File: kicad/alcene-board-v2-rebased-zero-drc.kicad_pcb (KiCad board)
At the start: 2 copper layers, 109.3 x 87.1 mm, 16 parts, among them J1 ESP32-S3-DevKitC-1_J1, J2 USB-C Input, J3 ESP32-S3-DevKitC-1_J3, J4 ILI9341_TFT_14pin, J5 Male Pin Header 1x18 - J1 Sig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, J6 Male Pin Header 1x18 - J3 Sig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, J7 Male Pin Header 2x4 - GND, J8 Male Pin Header 2x4 - 3V3, J9 Male Pin Header 2x4 - VIN 5V, SW1 ESP32-S3 Reset (NO momentary)

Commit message: feat: moving R and C positions
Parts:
- moved C1 25.5 mm to (123.0, 114.5), turned to -90 degrees
- moved C2 24.6 mm to (128.0, 114.5), turned to -90 degrees
- moved R2 23.8 mm to (126.2, 110.2)
- moved R1 23.4 mm to (121.7, 110.2)
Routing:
- net GND: track 240.2 -> 272.8 mm
- net Net-(J2-PadA5): track 2.33 -> 27.3 mm, vias 0 -> 2
- net VIN: track 167.5 -> 183.0 mm, vias 1 -> 3
- net Net-(J2-PadB5): track 10.2 -> 25.1 mm, vias 0 -> 1
- net GPIO19: track 51.3 -> 50.8 mm

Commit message: feat: update layouting
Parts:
- moved J7 1.27 mm to (129.7, 38.8)
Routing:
- net GND: track 272.8 -> 274.0 mm
- net GPIO14: track 75.4 -> 74.8 mm
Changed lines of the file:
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@@
 		(tags "USB Type-C Receptacle Through-hole Right angle")
 		(property "Reference" "J2"
-			(at 10.605 -4.49 0)
+			(at 3.355 -1.94 0)
 			(layer "F.SilkS")
 			(effects
@@
 	(footprint "Connector_PinHeader_2.54mm:PinHeader_2x04_P2.54mm_Vertical"
 		(layer "F.Cu")
-		(at 130.93 38.75 -90)
+		(at 129.66 38.75 -90)
 		(descr "Through hole straight pin header, 2x04, 2.54mm pitch, double rows")
 		(tags "Through hole pin header THT 2x04 2.54mm double row")
@@
 	)
 	(gr_text "3V3"
-		(at 110.51 36.1 0)
+		(at 107.97 36.1 0)
 		(layer "F.SilkS")
 		(effects
@@
 	)
 	(gr_text "GND"
-		(at 127.12 36.1 0)
+		(at 125.85 36.1 0)
 		(layer "F.SilkS")
 		(effects
@@
 	)
 	(segment
-		(start 123.31 41.29)
-		(end 130.93 41.29)
+		(start 149.245 111.84)
+		(end 150.585 111.84)
 		(width 0.2)
 		(layer "F.Cu")
@@
 	)
 	(segment
-		(start 149.245 111.84)
-		(end 150.585 111.84)
+		(start 122.04 38.75)
+		(end 129.66 38.75)
+		(width 0.2)
+		(layer "F.Cu")
+		(net "GND")
+	)
+	(segment
+		(start 122.04 41.29)
+		(end 129.66 41.29)
 		(width 0.2)
 		(layer "F.Cu")
@@
 	)
 	(segment
-		(start 123.31 38.75)
-		(end 130.93 38.75)
-		(width 0.2)
-		(layer "F.Cu")
-		(net "GND")
-	)
-	(segment
 		(start 126.75 107.688)
 		(end 126.2 108.238)
@@
 	)
 	(segment
-		(start 129.56 50)
-		(end 129.56 51.1517)
+		(start 123.11 44.31)
+		(end 128.41 44.31)
 		(width 0.2)
 		(layer "B.Cu")
@@
 	)
 	(segment
-		(start 124.46 44.31)
-		(end 128.41 44.31)
+		(start 149.59 103.34)
+		(end 150.585 104.335)
 		(width 0.2)
 		(layer "B.Cu")
@@
 	)
 	(segment
-		(start 149.59 103.34)
-		(end 150.585 104.335)
-		(width 0.2)
-		(layer "B.Cu")
-		(net "GND")
-	)
-	(segment
-		(start 123.31 41.29)
-		(end 123.31 43.16)
+		(start 122.04 43.24)
+		(end 123.11 44.31)
 		(width 0.2)
 		(layer "B.Cu")
@@
 	)
 	(segment
-		(start 128.402 52.0219)
-		(end 128.402 99.6419)
+		(start 129.56 50)
+		(end 129.56 50.89)
 		(width 0.2)
 		(layer "B.Cu")
@@
 	)
 	(segment
-		(start 130.93 41.29)
-		(end 130.93 38.75)
+		(start 129.56 45.46)
+		(end 129.56 50)
 		(width 0.2)
 		(layer "B.Cu")
@@
 	)
 	(segment
-		(start 129.56 45.46)
-		(end 129.56 50)
+		(start 128.402 52.048)
+		(end 128.402 99.6419)
 		(width 0.2)
 		(layer "B.Cu")
@@
 	)
 	(segment
-		(start 144.6 103.34)
-		(end 149.59 103.34)
+		(start 129.56 50.89)
+		(end 128.402 52.048)
 		(width 0.2)
 		(layer "B.Cu")
@@
 	)
 	(segment
-		(start 129.56 51.1517)
-		(end 129.272 51.1517)
+		(start 144.6 103.34)
+		(end 149.59 103.34)
 		(width 0.2)
 		(layer "B.Cu")
@@
 	)
 	(segment
-		(start 149.245 113.19)
-		(end 150.585 113.19)
+		(start 129.66 41.29)
+		(end 129.66 38.75)
 		(width 0.2)
 		(layer "B.Cu")
@@
 	)
 	(segment
-		(start 123.31 43.16)
-		(end 124.46 44.31)
+		(start 149.245 113.19)
+		(end 150.585 113.19)
 		(width 0.2)
 		(layer "B.Cu")
@@
 	)
 	(segment
-		(start 129.272 51.1517)
-		(end 128.402 52.0219)
+		(start 122.04 41.29)
+		(end 122.04 43.24)
 		(width 0.2)
 		(layer "B.Cu")
@@
 	)
 	(segment
-		(start 104.741 76.5803)
-		(end 103.674 76.5803)
+		(start 111.78 41.29)
+		(end 111.78 38.75)
 		(width 0.2)
 		(layer "B.Cu")
@@
 	)
 	(segment
-		(start 111.78 41.29)
-		(end 111.78 38.75)
+		(start 76.4871 112.7529)
+		(end 76.89 112.35)
 		(width 0.2)
 		(layer "B.Cu")
@@
 	)
 	(segment
-		(start 78.7357 112.098)
-		(end 101.464 89.37)
+		(start 75.99 113.25)
+		(end 75.99 117.3)
 		(width 0.2)
 		(layer "B.Cu")
@@
 	)
 	(segment
-		(start 75.99 113.25)
-		(end 75.99 117.3)
+		(start 104.16 50)
+		(end 104.16 41.29)
 		(width 0.2)
 		(layer "B.Cu")
@@
 	)
 	(segment
-		(start 101.464 89.37)
-		(end 105.31 89.37)
+		(start 103.674 76.5803)
+		(end 102.92 75.8263)
 		(width 0.2)
 		(layer "B.Cu")
@@
 	)
 	(segment
-		(start 104.16 50)
-		(end 104.16 41.29)
+		(start 102.92 75.8263)
+		(end 102.92 53.7799)
 		(width 0.2)
 		(layer "B.Cu")
@@
 	)
 	(segment
-		(start 105.31 77.148884)
-		(end 105.151116 76.99)
+		(start 104.68 89.37)
+		(end 105.31 88.74)
 		(width 0.2)
 		(layer "B.Cu")
@@
 	)
 	(segment
-		(start 76.4871 112.7529)
-		(end 76.89 112.35)
+		(start 105.31 77.148884)
+		(end 105.151116 76.99)
 		(width 0.2)
 		(layer "B.Cu")
@@
 	)
 	(segment
-		(start 102.92 75.8263)
-		(end 102.92 53.7799)
+		(start 101.464 89.37)
+		(end 104.68 89.37)
 		(width 0.2)
 		(layer "B.Cu")
@@
 	)
 	(segment
-		(start 105.31 89.37)
-		(end 105.31 77.148884)
+		(start 78.7357 112.098)
+		(end 101.464 89.37)
 		(width 0.2)
 		(layer "B.Cu")
@@
 	)
 	(segment
-		(start 76.4871 112.753)
-		(end 76.4871 112.7529)
+		(start 105.151116 76.99)
+		(end 105.151 76.99)
 		(width 0.2)
 		(layer "B.Cu")
@@
 	)
 	(segment
-		(start 78.4837 112.35)
-		(end 78.7357 112.098)
+		(start 104.741 76.5803)
+		(end 103.674 76.5803)
 		(width 0.2)
 		(layer "B.Cu")
@@
 	)
 	(segment
-		(start 105.151116 76.99)
-		(end 105.151 76.99)
+		(start 78.4837 112.35)
+		(end 78.7357 112.098)
 		(width 0.2)
 		(layer "B.Cu")
@@
 	)
 	(segment
-		(start 105.151 76.99)
-		(end 104.741 76.5803)
+		(start 75.99 113.25)
+		(end 76.4871 112.753)
 		(width 0.2)
 		(layer "B.Cu")
@@
 	)
 	(segment
+		(start 105.31 88.74)
+		(end 105.31 77.148884)
+		(width 0.2)
+		(layer "B.Cu")
+		(net "3V3")
+	)
+	(segment
 		(start 104.16 52.54)
 		(end 104.16 50)
@@
 	)
 	(segment
-		(start 75.99 113.25)
-		(end 76.4871 112.753)
+		(start 105.151 76.99)
+		(end 104.741 76.5803)
 		(width 0.2)
 		(layer "B.Cu")
@@
 	)
 	(segment
-		(start 103.674 76.5803)
-		(end 102.92 75.8263)
+		(start 76.4871 112.753)
+		(end 76.4871 112.7529)
 		(width 0.2)
 		(layer "B.Cu")
@@
 	)
 	(segment
-		(start 104.16 98.26)
-		(end 102.026 98.26)
+		(start 87.42 112.866)
+		(end 87.42 118.08)
 		(width 0.2)
 		(layer "B.Cu")
@@
 	)
 	(segment
-		(start 87.42 112.866)
-		(end 87.42 118.55)
+		(start 102.026 98.26)
+		(end 87.42 112.866)
+		(width 0.2)
+		(layer "B.Cu")
+		(net "GPIO14")
+	)
+	(segment
+		(start 87.42 118.08)
+		(end 86.95 118.55)
 		(width 0.2)
 		(layer "B.Cu")
@@
 	)
 	(segment
-		(start 87.42 118.55)
-		(end 83.61 118.55)
+		(start 86.95 118.55)
+		(end 84.2 118.55)
 		(width 0.2)
 		(layer "B.Cu")
@@
 	)
 	(segment
-		(start 83.61 118.55)
+		(start 83.61 117.96)
 		(end 83.61 117.3)
 		(width 0.2)
@@
 	)
 	(segment
-		(start 102.026 98.26)
-		(end 87.42 112.866)
+		(start 84.2 118.55)
+		(end 83.61 117.96)
+		(width 0.2)
+		(layer "B.Cu")
+		(net "GPIO14")
+	)
+	(segment
+		(start 104.16 98.26)
+		(end 102.026 98.26)
 		(width 0.2)
 		(layer "B.Cu")
@@
 	)
 	(segment
-		(start 143.848 85.602)
-		(end 143.848 57.0154)
+		(start 142.9383 86.5117)
+		(end 143.848 85.602)
 		(width 0.2)
 		(layer "B.Cu")
@@
 	)
 	(segment
-		(start 145 56.1517)
-		(end 145 55)
+		(start 143.848 57.065654)
+		(end 145 55.913654)
 		(width 0.2)
 		(layer "B.Cu")
@@
 	)
 	(segment
-		(start 142.9383 86.5117)
-		(end 143.848 85.602)
-		(width 0.2)
-		(layer "B.Cu")
-		(net "GPIO19")
-	)
-	(segment
-		(start 144.712 56.1517)
-		(end 145 56.1517)
+		(start 141.308 86.5117)
+		(end 142.9383 86.5117)
 		(width 0.2)
 		(layer "B.Cu")
@@
 	)
 	(segment
-		(start 141.308 86.5117)
-		(end 142.9383 86.5117)
+		(start 143.848 85.602)
+		(end 143.848 57.065654)
 		(width 0.2)
 		(layer "B.Cu")
@@
 	)
 	(segment
-		(start 143.848 57.0154)
-		(end 144.712 56.1517)
+		(start 145 55.913654)
+		(end 145 55)
 		(width 0.2)
 		(layer "B.Cu")

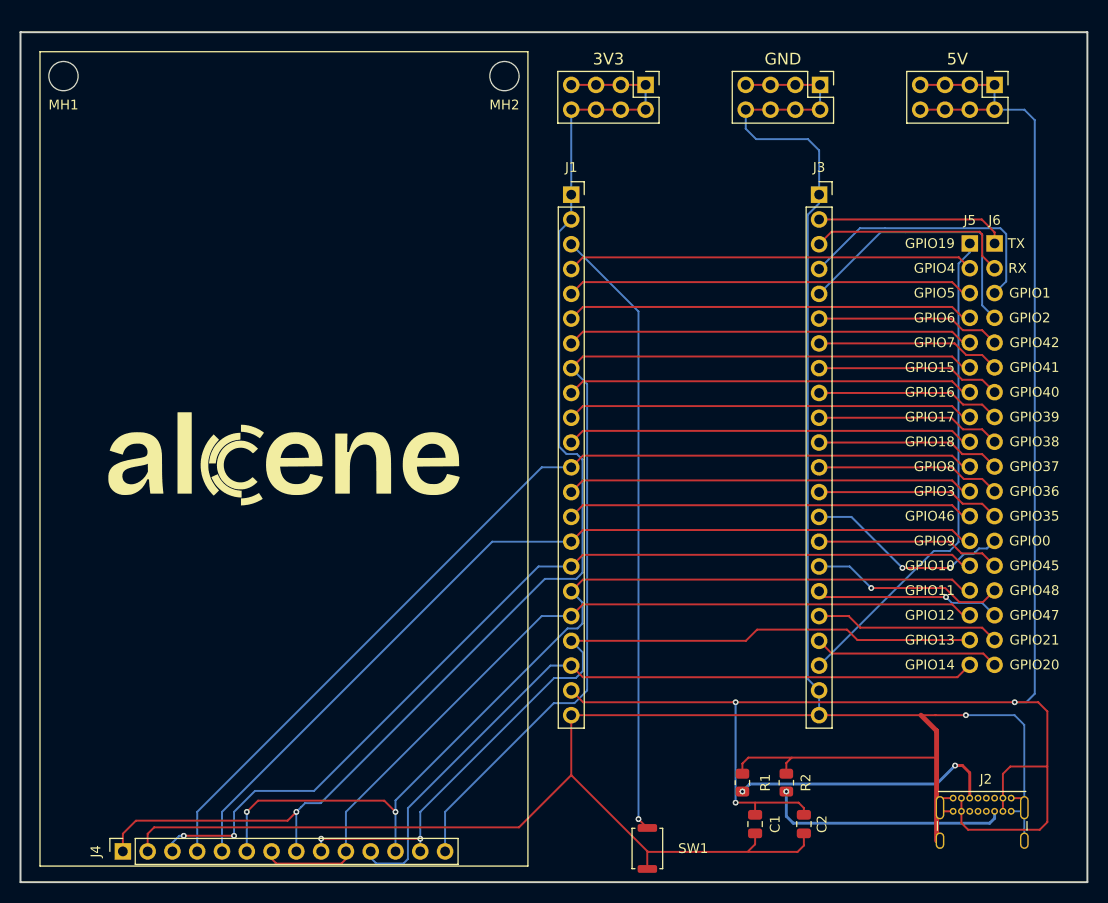
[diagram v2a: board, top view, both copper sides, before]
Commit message: feat: fixing 50x85 TFT layout
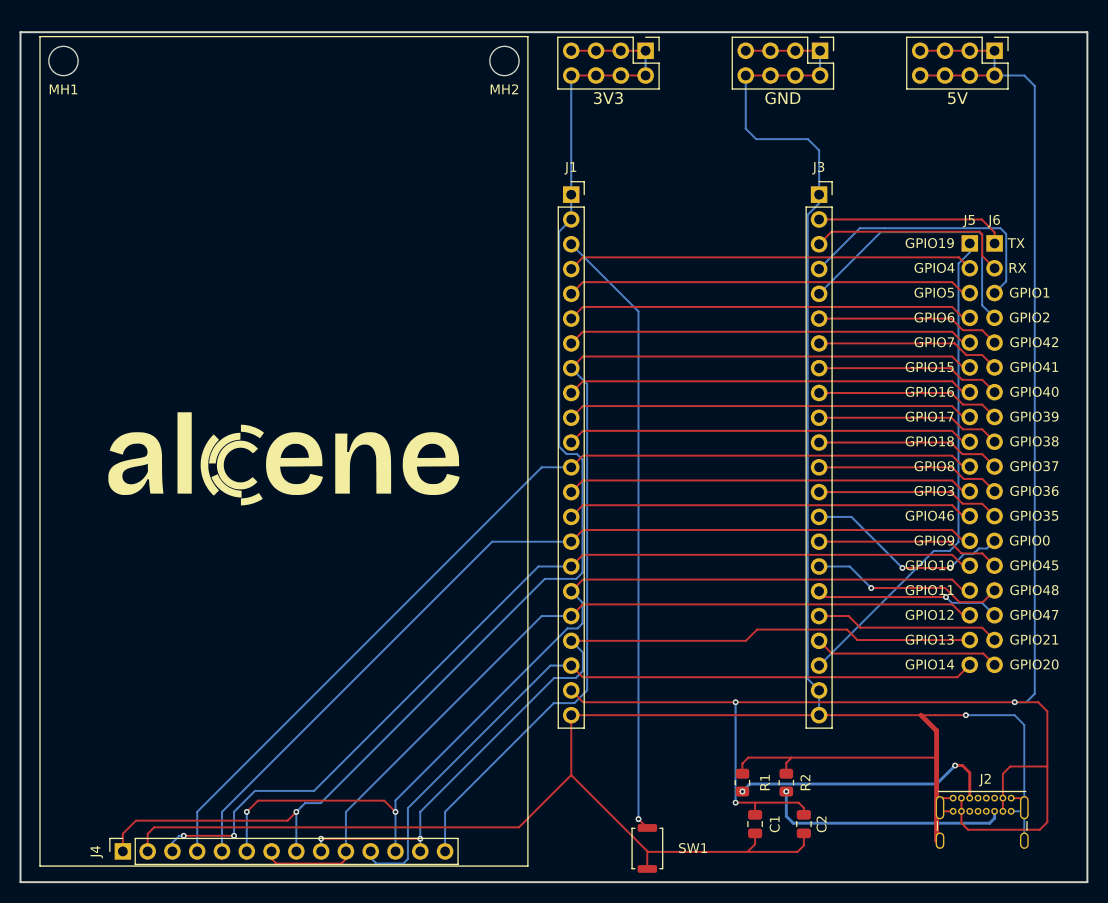
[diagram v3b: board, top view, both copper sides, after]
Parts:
- moved J7 3.50 mm to (129.7, 35.2)
- moved J8 3.50 mm to (111.8, 35.2)
- moved J9 3.50 mm to (147.5, 35.2)
- moved MH1 1.55 mm to (52.1, 36.3)
- moved MH2 1.55 mm to (97.3, 36.3)
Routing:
- net VIN: track 183.0 -> 186.5 mm
- net GND: track 274.0 -> 277.5 mm
- net 3V3: track 131.4 -> 134.9 mm
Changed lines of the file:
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@@
 	(footprint "MountingHole:MountingHole_3mm"
 		(layer "F.Cu")
-		(at 52.125 37.85)
+		(at 52.125 36.3)
 		(descr "Mounting Hole 3mm, no annular, generated by kicad-footprint-generator mountinghole.py")
 		(tags "mountinghole")
@@
 	(footprint "MountingHole:MountingHole_3mm"
 		(layer "F.Cu")
-		(at 97.315 37.85)
+		(at 97.315 36.3)
 		(descr "Mounting Hole 3mm, no annular, generated by kicad-footprint-generator mountinghole.py")
 		(tags "mountinghole")
@@
 	(footprint "Connector_PinHeader_2.54mm:PinHeader_2x04_P2.54mm_Vertical"
 		(layer "F.Cu")
-		(at 111.78 38.75 -90)
+		(at 111.78 35.25 -90)
 		(descr "Through hole straight pin header, 2x04, 2.54mm pitch, double rows")
 		(tags "Through hole pin header THT 2x04 2.54mm double row")
@@
 	(footprint "Connector_PinHeader_2.54mm:PinHeader_2x04_P2.54mm_Vertical"
 		(layer "F.Cu")
-		(at 129.66 38.75 -90)
+		(at 129.66 35.25 -90)
 		(descr "Through hole straight pin header, 2x04, 2.54mm pitch, double rows")
 		(tags "Through hole pin header THT 2x04 2.54mm double row")
@@
 	(footprint "Connector_PinHeader_2.54mm:PinHeader_2x04_P2.54mm_Vertical"
 		(layer "F.Cu")
-		(at 147.54 38.75 -90)
+		(at 147.54 35.25 -90)
 		(descr "Through hole straight pin header, 2x04, 2.54mm pitch, double rows")
 		(tags "Through hole pin header THT 2x04 2.54mm double row")
@@
 	)
 	(gr_rect
-		(start 49.72 35.35)
+		(start 49.72 33.8)
 		(end 99.72 118.8)
 		(stroke
@@
 	)
 	(gr_text "3V3"
-		(at 107.97 36.1 0)
+		(at 107.97 40.15 0)
 		(layer "F.SilkS")
 		(effects
@@
 	)
 	(gr_text "GND"
-		(at 125.85 36.1 0)
+		(at 125.85 40.15 0)
 		(layer "F.SilkS")
 		(effects
@@
 	)
 	(gr_text "5V"
-		(at 143.73 36.1 0)
+		(at 143.73 40.15 0)
 		(layer "F.SilkS")
 		(effects
@@
 	)
 	(segment
-		(start 122.312 107.688)
-		(end 121.7 108.3)
+		(start 122.04 35.25)
+		(end 129.66 35.25)
 		(width 0.2)
 		(layer "F.Cu")
@@
 	)
 	(segment
-		(start 129.56 103.34)
-		(end 104.16 103.34)
+		(start 122.312 107.688)
+		(end 121.7 108.3)
 		(width 0.2)
 		(layer "F.Cu")
@@
 	(segment
 		(start 129.56 103.34)
-		(end 141.49 103.34)
+		(end 104.16 103.34)
 		(width 0.2)
 		(layer "F.Cu")
@@
 	)
 	(segment
-		(start 149.245 111.84)
-		(end 150.585 111.84)
+		(start 122.04 37.79)
+		(end 129.66 37.79)
 		(width 0.2)
 		(layer "F.Cu")
@@
 	)
 	(segment
-		(start 122.04 38.75)
-		(end 129.66 38.75)
+		(start 129.56 103.34)
+		(end 141.49 103.34)
 		(width 0.2)
 		(layer "F.Cu")
@@
 	)
 	(segment
-		(start 122.04 41.29)
-		(end 129.66 41.29)
+		(start 149.245 111.84)
+		(end 150.585 111.84)
 		(width 0.2)
 		(layer "F.Cu")
@@
 	)
 	(segment
+		(start 129.66 37.79)
+		(end 129.66 35.25)
+		(width 0.2)
+		(layer "B.Cu")
+		(net "GND")
+	)
+	(segment
 		(start 129.56 103.34)
 		(end 129.56 100.8)
@@
 	)
 	(segment
+		(start 122.04 37.79)
+		(end 122.04 43.24)
+		(width 0.2)
+		(layer "B.Cu")
+		(net "GND")
+	)
+	(segment
 		(start 129.56 45.46)
 		(end 129.56 50)
@@
 	)
 	(segment
-		(start 129.66 41.29)
-		(end 129.66 38.75)
-		(width 0.2)
-		(layer "B.Cu")
-		(net "GND")
-	)
-	(segment
 		(start 149.245 113.19)
 		(end 150.585 113.19)
@@
 	)
 	(segment
-		(start 122.04 41.29)
-		(end 122.04 43.24)
-		(width 0.2)
-		(layer "B.Cu")
-		(net "GND")
-	)
-	(segment
 		(start 148.395 109.355)
 		(end 148.395 111.84)
@@
 	)
 	(segment
-		(start 139.92 41.29)
-		(end 147.54 41.29)
-		(width 0.2)
-		(layer "F.Cu")
-		(net "VIN")
-	)
-	(segment
 		(start 128 112.85)
 		(end 128 113.55)
@@
 	)
 	(segment
+		(start 139.92 35.25)
+		(end 147.54 35.25)
+		(width 0.2)
+		(layer "F.Cu")
+		(net "VIN")
+	)
+	(segment
+		(start 139.92 37.79)
+		(end 147.54 37.79)
+		(width 0.2)
+		(layer "F.Cu")
+		(net "VIN")
+	)
+	(segment
 		(start 105.373 102.013)
 		(end 149.6 102.013)
@@
 	)
 	(segment
-		(start 139.92 38.75)
-		(end 147.54 38.75)
-		(width 0.2)
-		(layer "F.Cu")
-		(net "VIN")
-	)
-	(segment
 		(start 104.16 100.8)
 		(end 105.373 102.013)
@@
 	)
 	(segment
-		(start 147.54 41.29)
-		(end 147.54 38.75)
+		(start 151.66 38.86)
+		(end 151.66 101.14)
 		(width 0.2)
 		(layer "B.Cu")
@@
 	)
 	(segment
-		(start 151.66 42.36)
-		(end 151.66 101.14)
+		(start 147.54 37.79)
+		(end 147.54 35.25)
 		(width 0.2)
 		(layer "B.Cu")
@@
 	)
 	(segment
-		(start 150.59 41.29)
-		(end 151.66 42.36)
+		(start 150.59 37.79)
+		(end 151.66 38.86)
 		(width 0.2)
 		(layer "B.Cu")
@@
 	)
 	(segment
-		(start 147.54 41.29)
-		(end 150.59 41.29)
+		(start 147.54 37.79)
+		(end 150.59 37.79)
 		(width 0.2)
 		(layer "B.Cu")
@@
 	)
 	(segment
-		(start 104.16 41.29)
-		(end 111.78 41.29)
+		(start 59.55 114.15)
+		(end 58.21 115.49)
 		(width 0.2)
 		(layer "F.Cu")
@@
 	)
 	(segment
-		(start 104.16 38.75)
-		(end 111.78 38.75)
+		(start 75.09 114.15)
+		(end 59.55 114.15)
 		(width 0.2)
 		(layer "F.Cu")
@@
 	)
 	(segment
-		(start 59.55 114.15)
-		(end 58.21 115.49)
+		(start 58.21 115.49)
+		(end 58.21 117.3)
 		(width 0.2)
 		(layer "F.Cu")
@@
 	)
 	(segment
-		(start 75.09 114.15)
-		(end 59.55 114.15)
+		(start 75.99 113.25)
+		(end 75.09 114.15)
 		(width 0.2)
 		(layer "F.Cu")
@@
 	)
 	(segment
-		(start 58.21 115.49)
-		(end 58.21 117.3)
+		(start 104.16 35.25)
+		(end 111.78 35.25)
 		(width 0.2)
 		(layer "F.Cu")
@@
 	)
 	(segment
-		(start 75.99 113.25)
-		(end 75.09 114.15)
+		(start 104.16 37.79)
+		(end 111.78 37.79)
 		(width 0.2)
 		(layer "F.Cu")
@@
 	)
 	(segment
-		(start 111.78 41.29)
-		(end 111.78 38.75)
-		(width 0.2)
-		(layer "B.Cu")
-		(net "3V3")
-	)
-	(segment
 		(start 76.4871 112.7529)
 		(end 76.89 112.35)
@@
 	(segment
 		(start 104.16 50)
-		(end 104.16 41.29)
+		(end 104.16 52.54)
 		(width 0.2)
 		(layer "B.Cu")
@@
 	)
 	(segment
+		(start 111.78 37.79)
+		(end 111.78 35.25)
+		(width 0.2)
+		(layer "B.Cu")
+		(net "3V3")
+	)
+	(segment
 		(start 102.92 53.7799)
 		(end 104.16 52.54)
@@
 	)
 	(segment
+		(start 104.16 37.79)
+		(end 104.16 50)
+		(width 0.2)
+		(layer "B.Cu")
+		(net "3V3")
+	)
+	(segment
 		(start 105.151116 76.99)
 		(end 105.151 76.99)
@@
 		(width 0.2)
 		(layer "B.Cu")
-		(net "3V3")
-	)
-	(segment
-		(start 104.16 52.54)
-		(end 104.16 50)
-		(width 0.2)
-		(layer "B.Cu")

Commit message: feat: final layout r2
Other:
- board size 109.3 x 87.1 mm -> 108 x 88.3 mm
